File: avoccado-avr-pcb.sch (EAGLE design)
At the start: 29 parts, among them IC1 MCP1703CB, Q1 #MHz, Q2 MOSFET-NCHANNEL2N7002PW, U1 ATMEGA168#, U2 MCP73831, X1 Micro USB

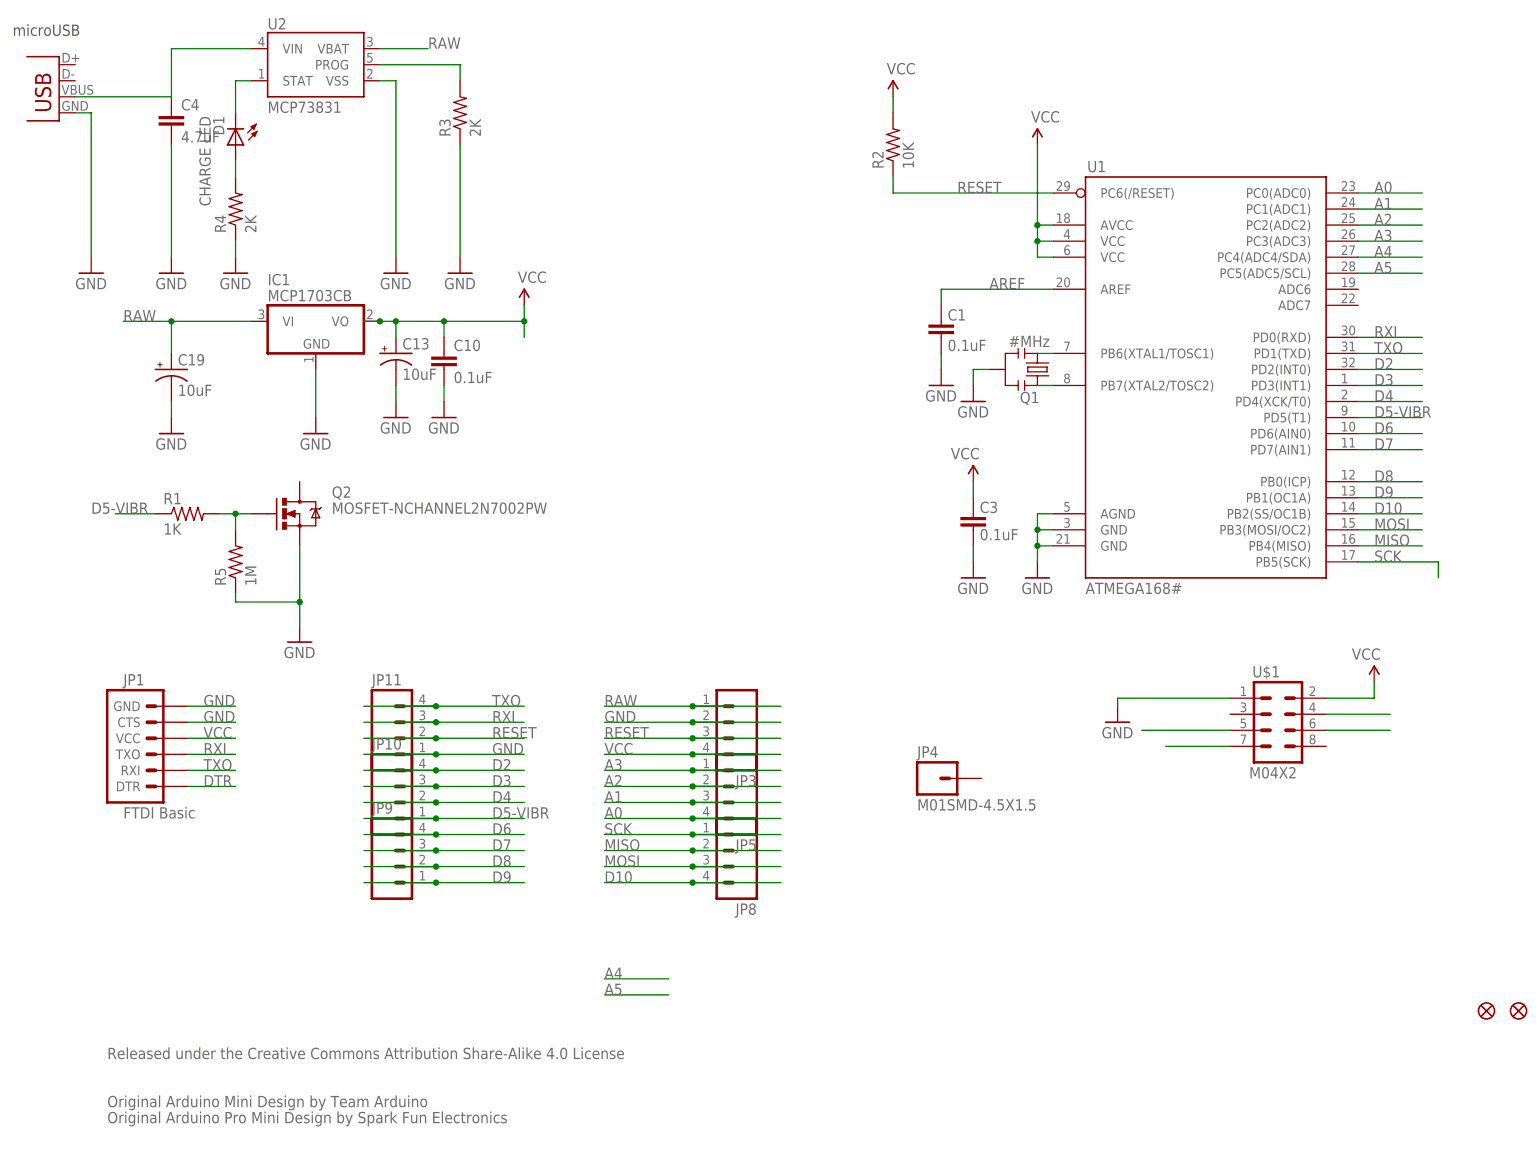
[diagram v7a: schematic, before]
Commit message: reroute NRF24 header with bottom layer, add MPU6050 satellite board
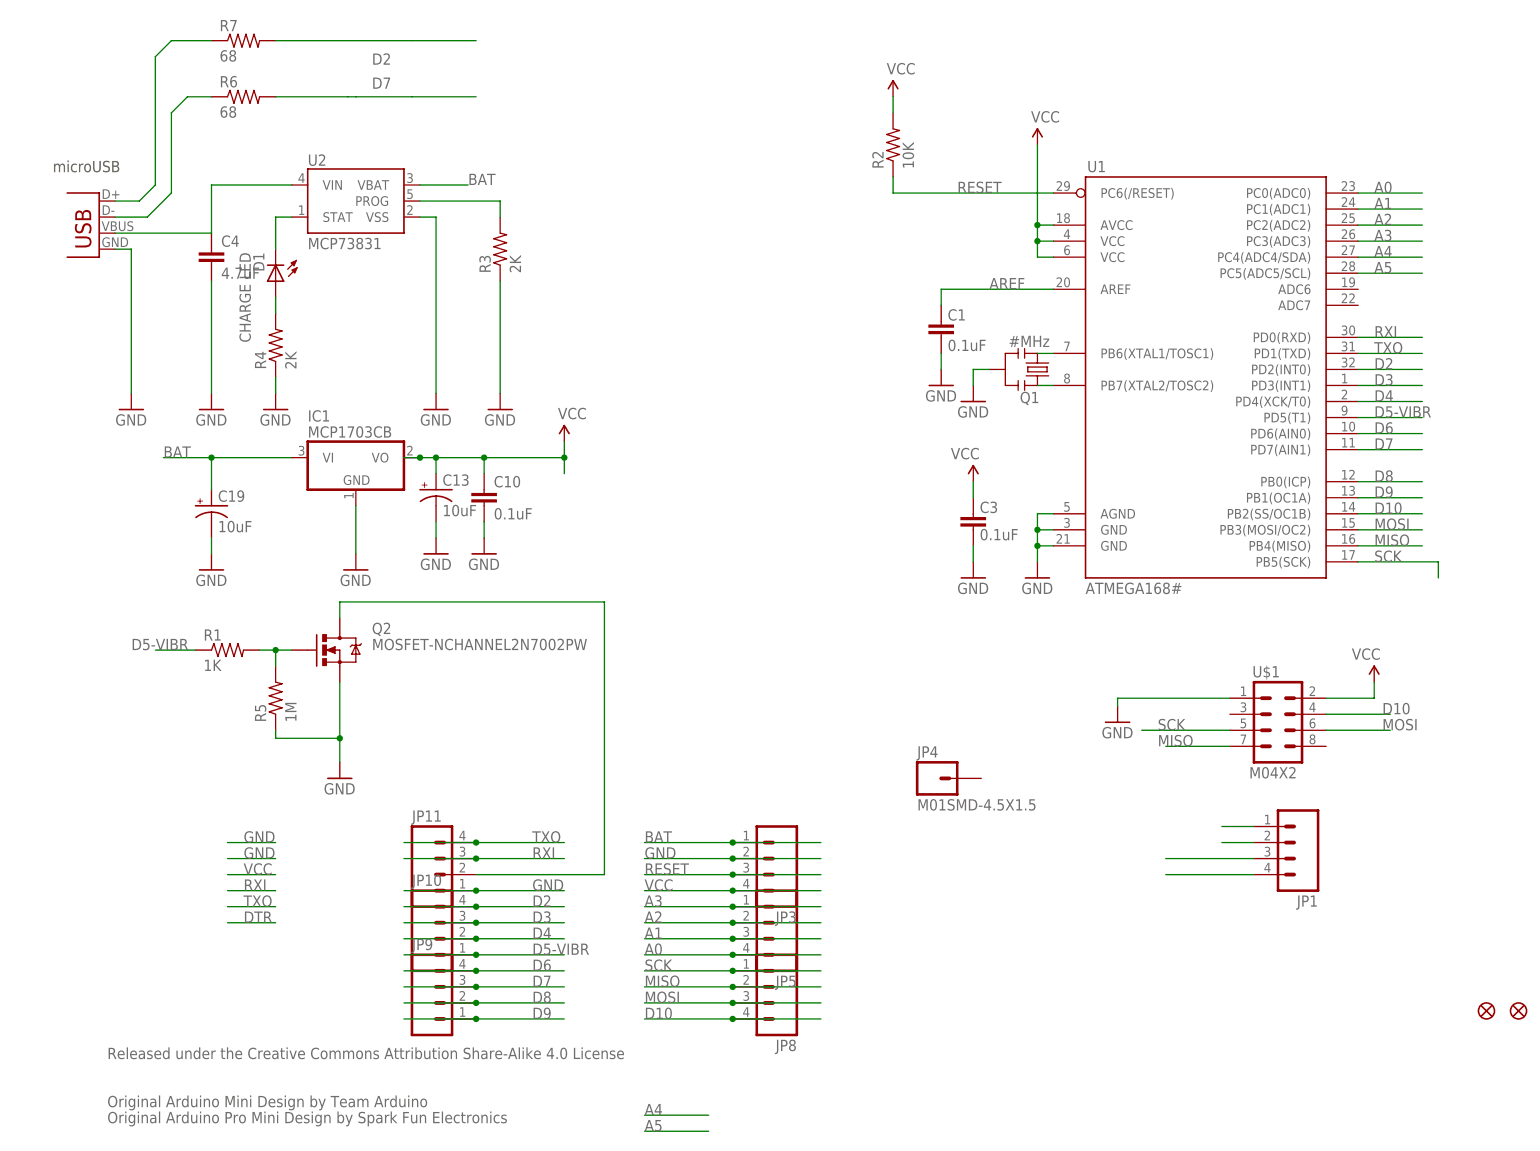
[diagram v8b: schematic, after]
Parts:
- added R6, R7: 68, SparkFun-Resistors:RESISTOR0603
- JP1: value FTDI Basic -> (none); device SparkFun:ARDUINO_SERIAL_PROGRAMPTH -> SparkFun-Connectors:M04LOCK
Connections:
- net RAW renamed BAT
- net VIN1 renamed BUS
- removed net DTR: JP1.DTR
- new net N$7: R7.1, X1.D+
- new net N$8: R6.1, X1.D-
- new net VIBR: JP11.2, Q2.D
- net A4: now also JP1.4
- net A5: now also JP1.3
- net D2: now also R7.2
- net D7: now also R6.2
- net GND: now also JP1.1; no longer JP1.CTS, JP1.GND
- net RESET: no longer JP11.2
- net RXI: no longer JP1.TXO
- net TXO: no longer JP1.RXI
- net VCC: now also JP1.2; no longer JP1.VCC
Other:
- moved on the sheet: C10, C13, C19, C4, D1, IC1, JP10, JP11, JP3, JP5, JP8, JP9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
